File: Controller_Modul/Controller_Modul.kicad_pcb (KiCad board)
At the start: 2 copper layers, 123 parts, among them J101 Screw_Terminal_01x02, J102 Conn_02x01, J103 Conn_01x06_Male, J104 Conn_02x01, J105 Conn_01x04_Male, J106 Conn_01x08_Male, J107 Micro_SD_Card_Det, J108 Screw_Terminal_01x04, J109 Conn_02x20_Odd_Even, J110 USB_B_Mini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

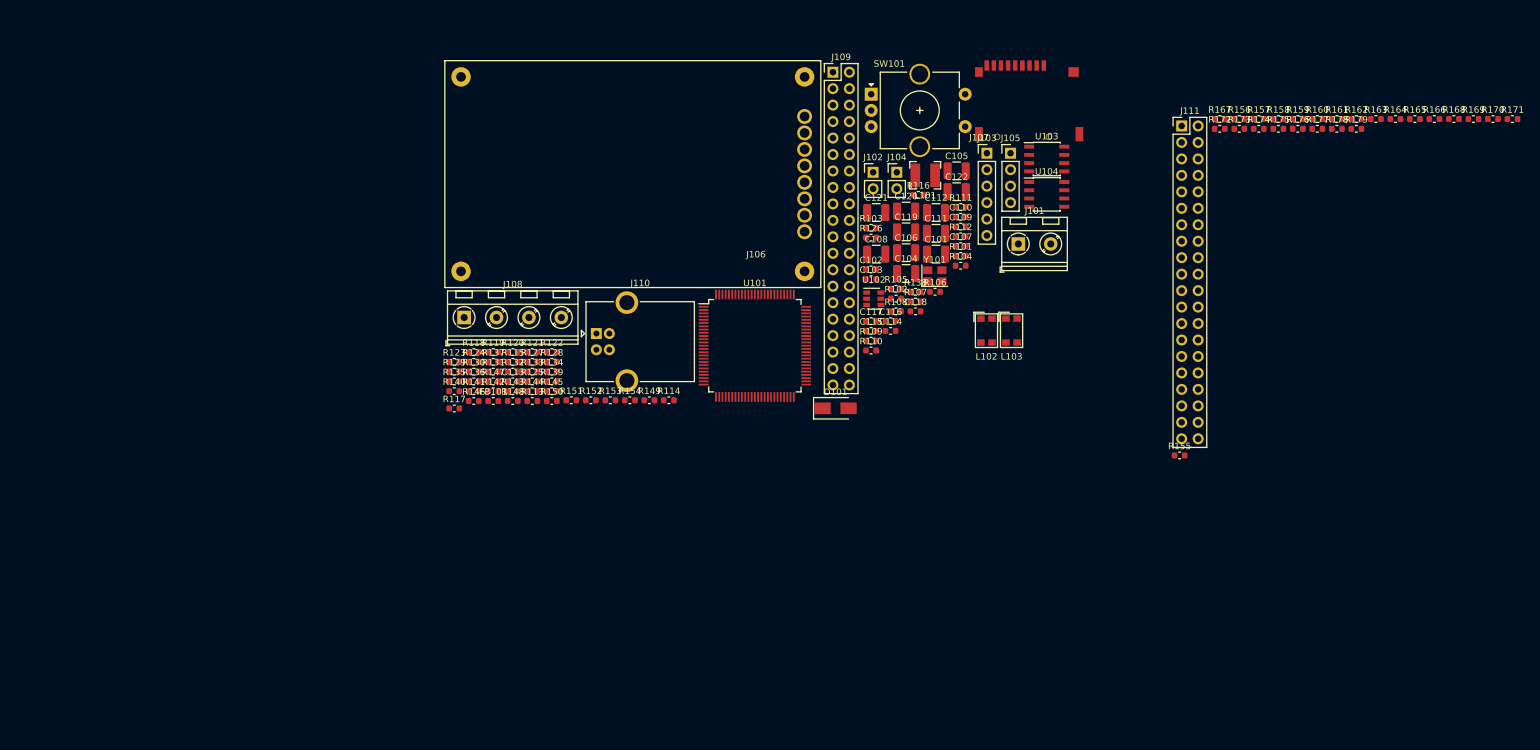
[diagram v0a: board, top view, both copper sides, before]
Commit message: Controller Board geplaced
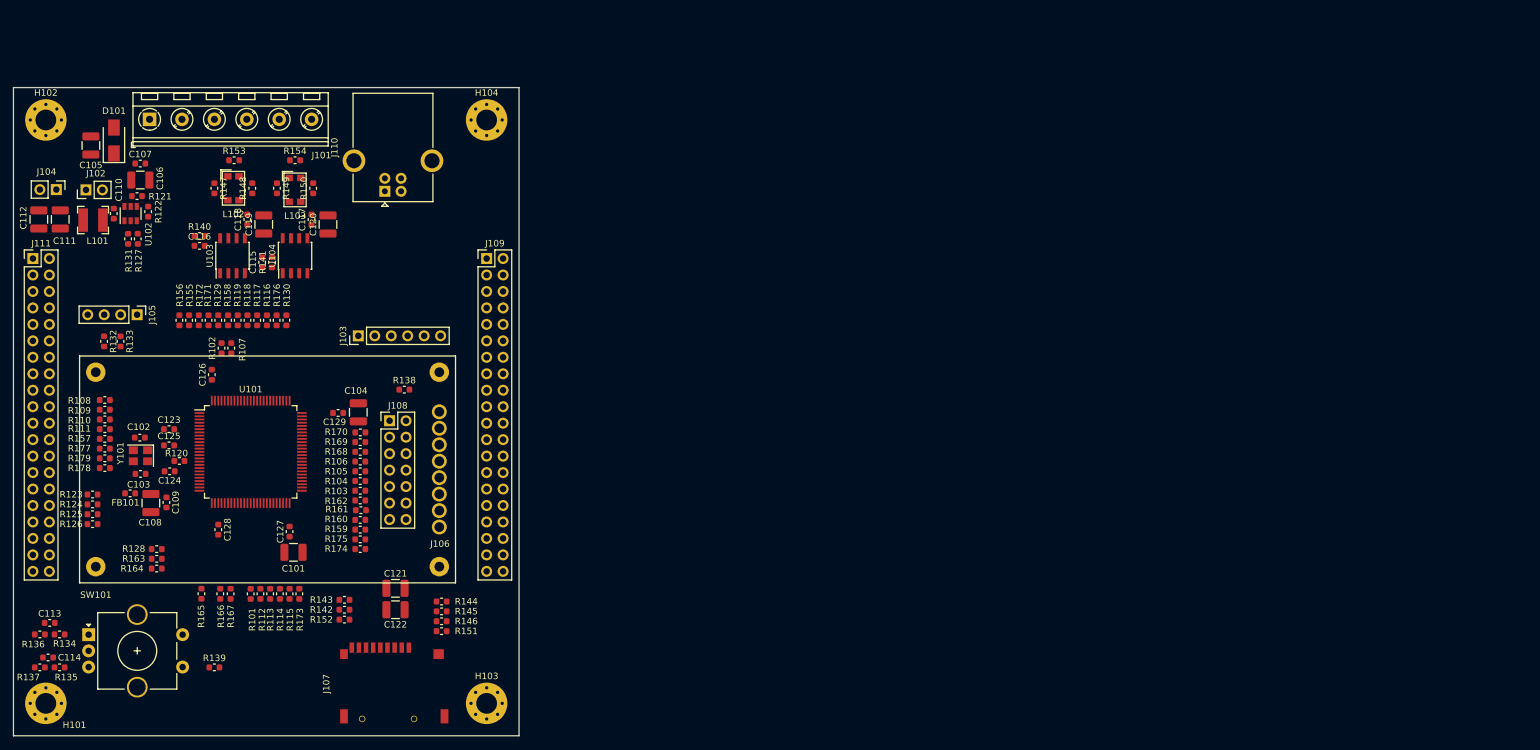
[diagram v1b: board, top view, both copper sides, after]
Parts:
- added C123: 100n 50V, Capacitor_SMD:C_0603_1608Metric, F.Cu at (104.0, 102.7)
- added C124: 100n 50V, Capacitor_SMD:C_0603_1608Metric, F.Cu at (104.1, 109.2)
- added C125: 100n 50V, Capacitor_SMD:C_0603_1608Metric, F.Cu at (104.0, 105.2)
- added C126: 100n 50V, Capacitor_SMD:C_0603_1608Metric, F.Cu at (110.6, 94.3)
- added C127: 100n 50V, Capacitor_SMD:C_0603_1608Metric, F.Cu at (122.6, 118.5)
- added C128: 100n 50V, Capacitor_SMD:C_0603_1608Metric, F.Cu at (111.6, 118.2)
- added C129: 100n 50V, Capacitor_SMD:C_0603_1608Metric, F.Cu at (130.1, 100.2)
- added H101: MountingHole_Pad, MountingHole:MountingHole_3.2mm_M3_Pad_Via, F.Cu at (85.0, 145.0)
- added H102: MountingHole_Pad, MountingHole:MountingHole_3.2mm_M3_Pad_Via, F.Cu at (85.0, 55.0)
- added H103: MountingHole_Pad, MountingHole:MountingHole_3.2mm_M3_Pad_Via, F.Cu at (153.0, 145.0)
- added H104: MountingHole_Pad, MountingHole:MountingHole_3.2mm_M3_Pad_Via, F.Cu at (153.0, 55.0)
- J101: value Screw_Terminal_01x02 -> Screw_Terminal_01x06; footprint TerminalBlock_RND:TerminalBlock_RND_205-00045_1x02_P5.00mm_Horizontal -> TerminalBlock_RND:TerminalBlock_RND_205-00049_1x06_P5.00mm_Horizontal
- J108: value Screw_Terminal_01x04 -> Conn_02x07_Odd_Even; footprint TerminalBlock_RND:TerminalBlock_RND_205-00047_1x04_P5.00mm_Horizontal -> Connector_PinHeader_2.54mm:PinHeader_2x07_P2.54mm_Vertical
- moved R171 203.5 mm to (110.1, 85.9), turned to 90 degrees
- moved R164 203.3 mm to (102.1, 124.2), turned to 180 degrees
- moved R166 201.1 mm to (111.9, 128.1), turned to 90 degrees
- moved R165 201.0 mm to (109.0, 128.1), turned to 270 degrees
- moved R163 199.9 mm to (102.1, 122.7), turned to 180 degrees
- moved R179 199.7 mm to (94.1, 107.2), turned to 180 degrees
- moved R178 197.1 mm to (94.1, 108.7), turned to 180 degrees
- moved R177 193.5 mm to (94.1, 105.7), turned to 180 degrees
- moved R157 184.7 mm to (94.1, 104.2)
- moved R170 181.3 mm to (133.5, 103.2)
- moved R169 178.8 mm to (133.5, 104.7)
- moved J111 178.4 mm to (83.0, 76.4)
- moved R168 176.4 mm to (133.5, 106.2)
- moved R167 169.3 mm to (113.5, 128.1), turned to 270 degrees
- moved R156 166.4 mm to (105.6, 85.9), turned to 270 degrees
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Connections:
- J108 pad 1: /CAN1_H -> +3V3
- J108 pad 2: /CAN1_L -> GND
- J108 pad 3: /CAN2_H -> /DISP_DIN
- J108 pad 4: /CAN2_L -> /DISP_CLK
- L102 pad 1: /CAN1_H -> Net-(L102-Pad1)
- L102 pad 2: Net-(L102-Pad2) -> /CAN1_H
- L102 pad 3: /CAN1_L -> Net-(L102-Pad3)
- L102 pad 4: Net-(L102-Pad4) -> /CAN1_L
- L103 pad 1: /CAN2_H -> Net-(L103-Pad1)
- L103 pad 2: Net-(L103-Pad2) -> /CAN2_H
- L103 pad 3: /CAN2_L -> Net-(L103-Pad3)
- L103 pad 4: Net-(L103-Pad4) -> /CAN2_L
- R147 pad 2: Net-(L102-Pad2) -> Net-(L102-Pad1)
- R148 pad 1: Net-(L102-Pad4) -> Net-(L102-Pad3)
- R149 pad 2: Net-(L103-Pad2) -> Net-(L103-Pad1)
- R150 pad 1: Net-(L103-Pad4) -> Net-(L103-Pad3)
- U103 pad 6: Net-(L102-Pad4) -> Net-(L102-Pad3)
- U103 pad 7: Net-(L102-Pad2) -> Net-(L102-Pad1)
- U104 pad 6: Net-(L103-Pad4) -> Net-(L103-Pad3)
- U104 pad 7: Net-(L103-Pad2) -> Net-(L103-Pad1)
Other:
- board outline added: 78 x 100 mm
- copper layers 2 -> 4
- net class Default: clearance 0.2 -> 0.1
- rule trace_clearance: 0.2 -> 0.1
- rule trace_min: 0.2 -> 0.15
- rule via_min_drill: 0.3 -> 0.2

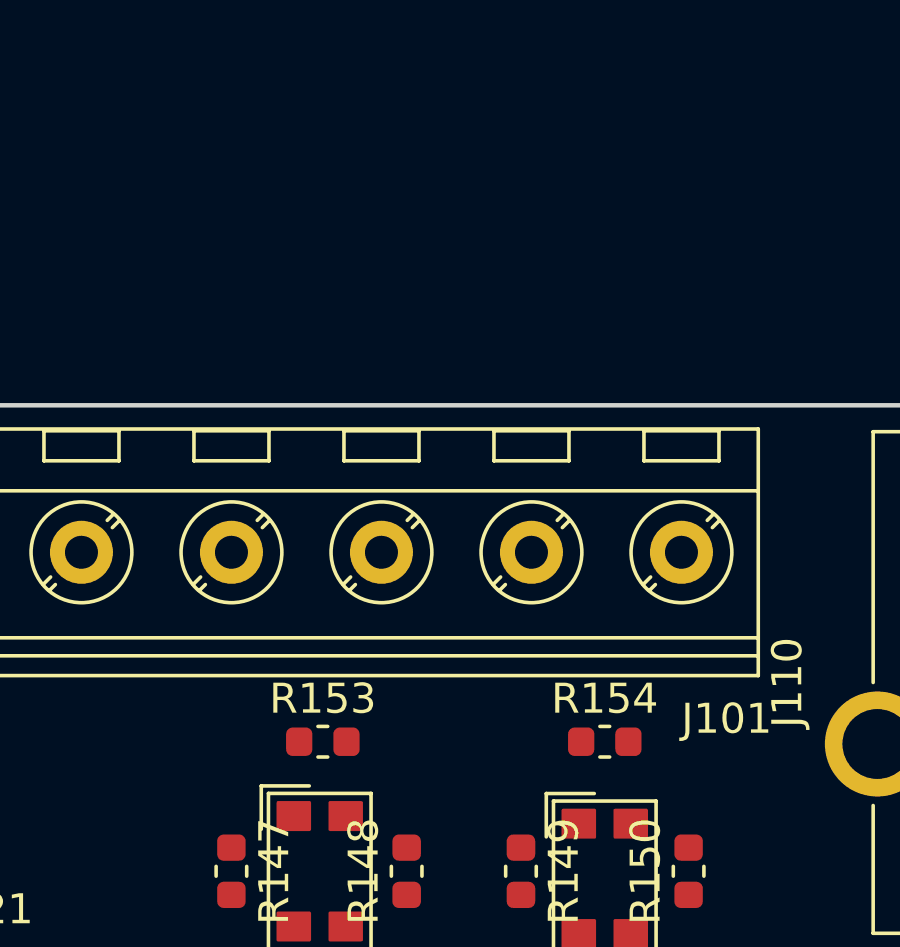
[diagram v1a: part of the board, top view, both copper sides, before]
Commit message: Controller Modul und CV Modul Can schaltung berichtigt. CV Modul abgerundete Ecken r=5mm. TODO: IO Modul, Feeder-Steckplätze, Display Modul
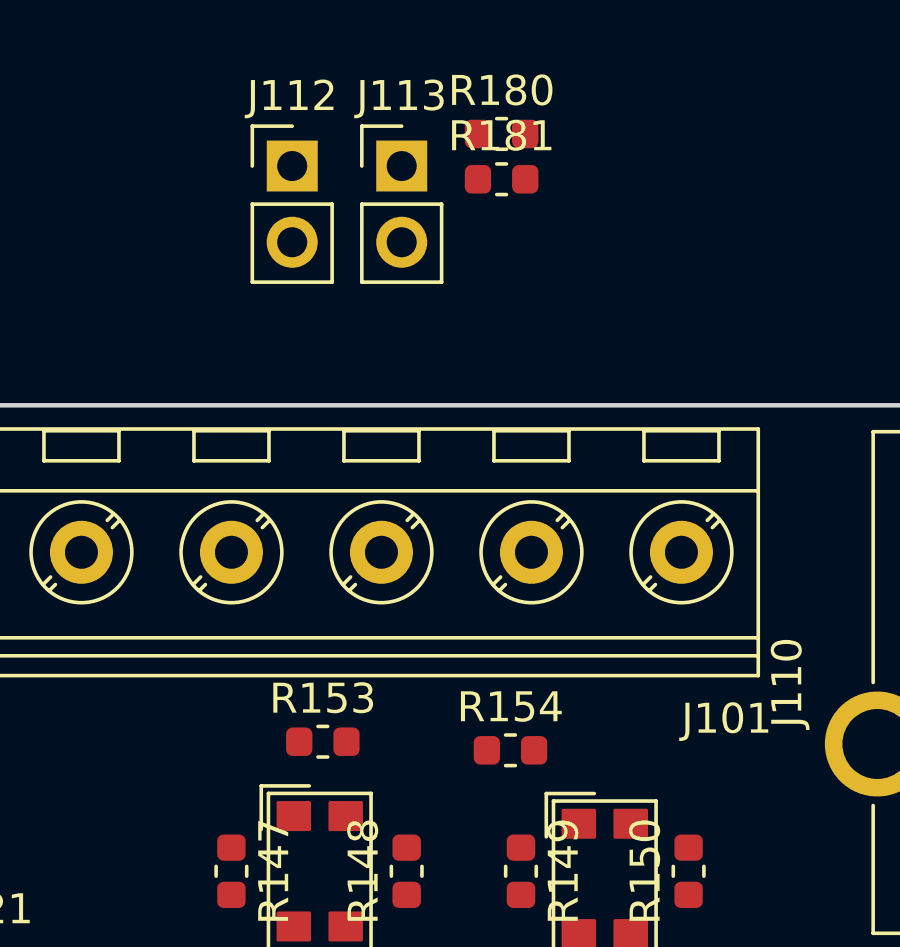
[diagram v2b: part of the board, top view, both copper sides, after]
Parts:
- added J112: Conn_02x01, Connector_PinHeader_2.54mm:PinHeader_1x02_P2.54mm_Vertical, F.Cu at (113.0, 42.0)
- added J113: Conn_02x01, Connector_PinHeader_2.54mm:PinHeader_1x02_P2.54mm_Vertical, F.Cu at (116.7, 42.0)
- added R180: DNP, Resistor_SMD:R_0603_1608Metric, F.Cu at (120.0, 41.0)
- added R181: DNP, Resistor_SMD:R_0603_1608Metric, F.Cu at (120.0, 42.5)
- U103, U104: value SN65HVD230DR -> SN65HVD230
- moved R154 3.16 mm to (120.3, 61.5)
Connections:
- R140 pad 1: +3V3 -> Net-(R140-Pad1)
- R140 pad 2: Net-(R140-Pad2) -> GND
- R141 pad 1: +3V3 -> Net-(R141-Pad1)
- R141 pad 2: Net-(R141-Pad2) -> GND
- R153 pad 2: /CAN1_L -> Net-(J112-Pad1)
- R154 pad 2: /CAN2_L -> Net-(J113-Pad1)
- U103 pad 5: +3V3 -> (no net)
- U103 pad 8: Net-(R140-Pad2) -> Net-(R140-Pad1)
- U104 pad 5: +3V3 -> (no net)
- U104 pad 8: Net-(R141-Pad2) -> Net-(R141-Pad1)

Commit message: IO-Modul fertig
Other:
- outline, holes or cut-outs redrawn
- board text added: "Controller Modul V0.1"

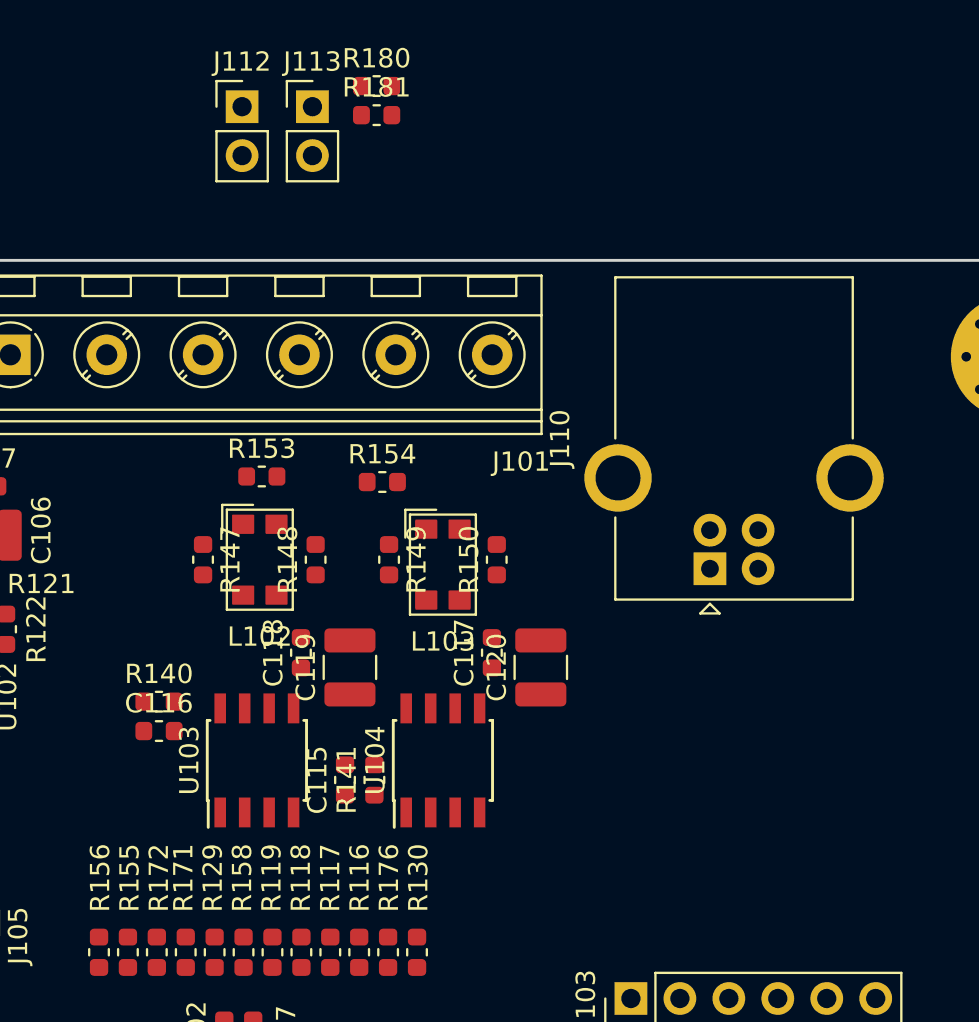
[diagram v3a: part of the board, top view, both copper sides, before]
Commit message: Feeder Microswitch für Tape Motor hinzugefügt. Einige 3D Step Modelle hinzugefügt. Stepper Board die Ecken abgerundet.
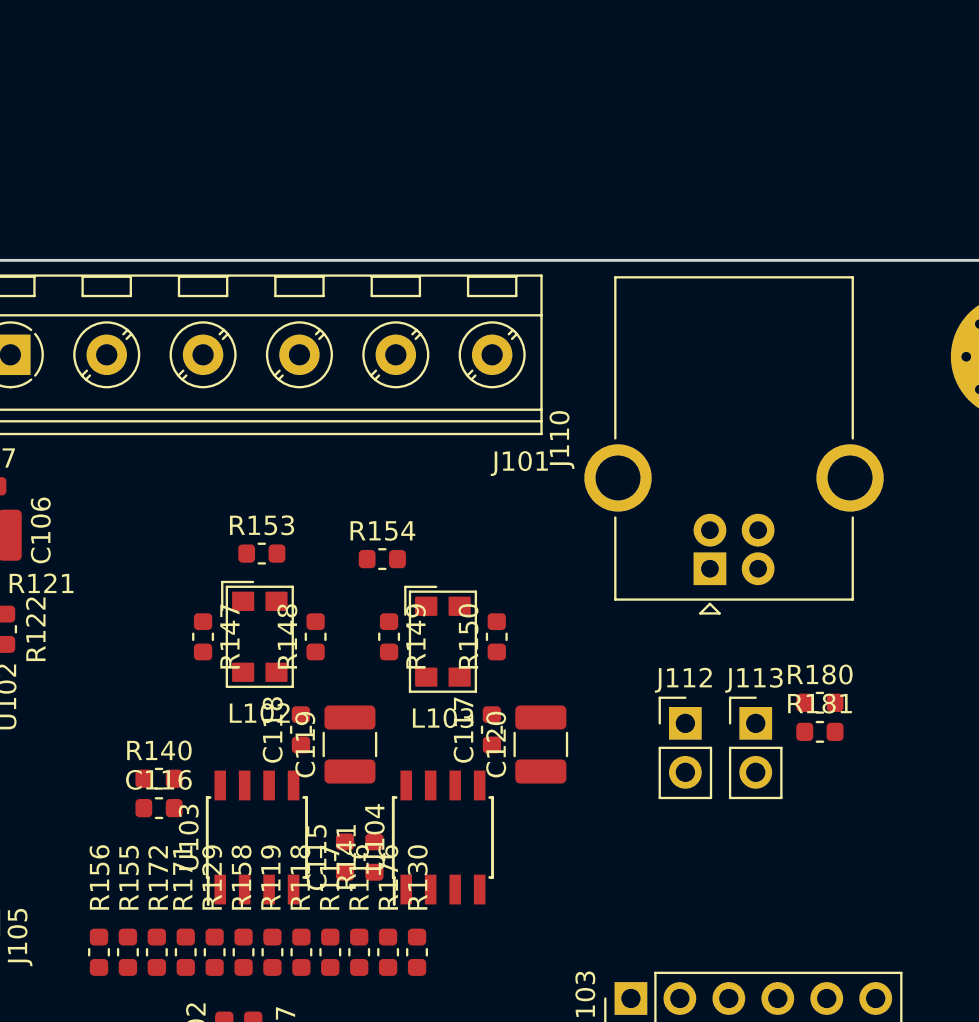
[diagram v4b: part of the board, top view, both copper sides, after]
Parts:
- moved J113 39.4 mm to (139.7, 74.0)
- moved J112 39.4 mm to (136.0, 74.0)
- moved R181 39.4 mm to (143.0, 74.5)
- moved R180 39.4 mm to (143.0, 73.0)
- moved C115 4.00 mm to (118.4, 81.0)
- moved C116 4.00 mm to (108.7, 78.4)
- moved C117 4.00 mm to (126.0, 74.4)
- moved C118 4.00 mm to (116.1, 74.4)
- moved C119 4.00 mm to (118.6, 75.1)
- moved C120 4.00 mm to (128.5, 75.1)
- moved L102 4.00 mm to (113.9, 69.5)
- moved L103 4.00 mm to (123.4, 69.8)
- moved R140 4.00 mm to (108.7, 76.9)
- moved R141 4.00 mm to (119.9, 81.0)
- moved R147 4.00 mm to (111.0, 69.5)
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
